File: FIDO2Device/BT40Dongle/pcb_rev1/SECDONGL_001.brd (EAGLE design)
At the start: 20.4 x 30 mm, 37 parts, among them CN1 CX60-24S-UNIT, CN2 IF_5PIN_H, CN3 IF_2PIN_SOL, SW1 SKRPACE010, SW2 SKTADAE010, U1 BT40, U2 ADP122ACPZ-3.3-R7, U3 RV-3028-C7

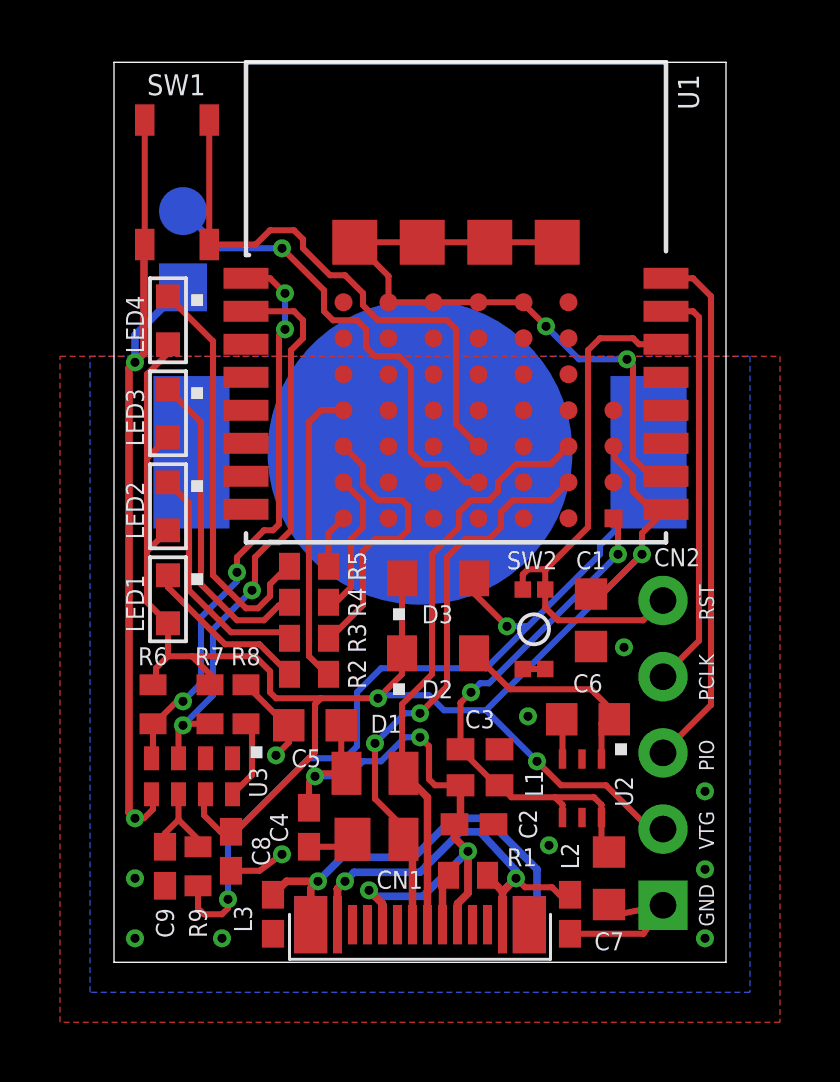
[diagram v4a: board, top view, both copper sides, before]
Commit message: 配線レイアウトを修正
・小修正
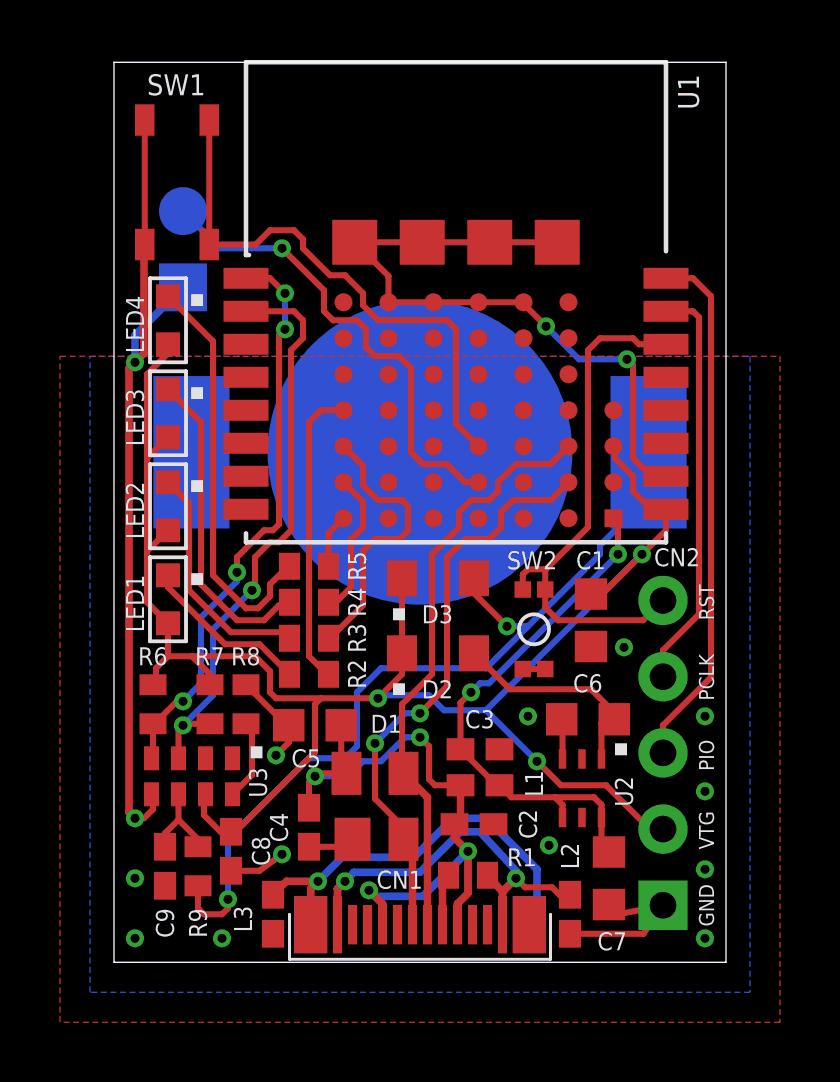
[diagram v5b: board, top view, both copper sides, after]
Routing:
- net 0V: vias 15 -> 16
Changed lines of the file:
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@@
 </element>
 <element name="C7" library="Parts" package="C0603K" value="1uF" x="16.5" y="2.8" smashed="yes" rot="R270">
-<attribute name="NAME" x="17" y="1" size="0.6" layer="25" rot="R180"/>
+<attribute name="NAME" x="17.1" y="1" size="0.6" layer="25" rot="R180"/>
 <attribute name="VALUE" x="15.00875" y="3.6" size="0.7112" layer="27" rot="R270"/>
 </element>
@@
 <wire x1="2.3" y1="22.5" x2="0.7" y2="20.9" width="0.254" layer="16"/>
 <wire x1="0.7" y1="20.9" x2="0.7" y2="20" width="0.254" layer="16"/>
+<via x="19.7" y="8.2" extent="1-16" drill="0.3"/>
 </signal>
 <signal name="VBUS_NRF">
@@
 <wire x1="16.375" y1="12.375" x2="16" y2="12.375" width="0.2032" layer="1"/>
 <wire x1="16" y1="12.375" x2="15.9" y2="12.275" width="0.2032" layer="1"/>
-<wire x1="17.6" y1="13.6" x2="17.6" y2="14.3" width="0.2032" layer="1"/>
-<wire x1="17.6" y1="14.3" x2="18.4" y2="15.1" width="0.2032" layer="1"/>
 <wire x1="16.65" y1="17.2" x2="16.7" y2="17.15" width="0.2032" layer="1"/>
 <wire x1="16.7" y1="17.15" x2="16.7" y2="16.8" width="0.2032" layer="1"/>
@@
 <wire x1="1.8" y1="10.2" x2="1.8" y2="11.3" width="0.2032" layer="1"/>
 <wire x1="1.1" y1="19.6" x2="1.1" y2="16.8" width="0.2032" layer="1"/>
-<wire x1="1.1" y1="16.5" x2="1.1" y2="13.7" width="0.2032" layer="1"/>
+<wire x1="1.1" y1="16.8" x2="1.1" y2="13.7" width="0.2032" layer="1"/>
 <wire x1="1.1" y1="13.7" x2="1.1" y2="12" width="0.2032" layer="1"/>
 <wire x1="1.1" y1="12" x2="1.8" y2="11.3" width="0.2032" layer="1"/>
 <wire x1="1.8" y1="14.4" x2="1.1" y2="13.7" width="0.2032" layer="1"/>
 <wire x1="1.8" y1="17.5" x2="1.1" y2="16.8" width="0.2032" layer="1"/>
-<wire x1="1.1" y1="16.8" x2="1.1" y2="16.5" width="0.2032" layer="1"/>
+<wire x1="17.6" y1="13.6" x2="18.4" y2="14.4" width="0.2032" layer="1"/>
+<wire x1="18.4" y1="14.4" x2="18.4" y2="15.1" width="0.2032" layer="1"/>
 </signal>
 <signal name="SW1">
@@
 <contactref element="U1" pad="16"/>
 <contactref element="CN2" pad="3"/>
-<wire x1="18.3" y1="6.98" x2="19.9" y2="8.58" width="0.2032" layer="1"/>
-<wire x1="19.9" y1="8.58" x2="19.9" y2="22.2" width="0.2032" layer="1"/>
+<wire x1="19.9" y1="9.5" x2="19.9" y2="22.2" width="0.2032" layer="1"/>
 <wire x1="18.4" y1="22.8" x2="19.3" y2="22.8" width="0.2032" layer="1"/>
 <wire x1="19.9" y1="22.2" x2="19.3" y2="22.8" width="0.2032" layer="1"/>
+<wire x1="18.3" y1="6.98" x2="18.3" y2="7.9" width="0.2032" layer="1"/>
+<wire x1="18.3" y1="7.9" x2="19.9" y2="9.5" width="0.2032" layer="1"/>
 </signal>
 <signal name="SWCLK">
 <contactref element="U1" pad="15"/>
 <contactref element="CN2" pad="4"/>
-<wire x1="18.3" y1="9.52" x2="19.5" y2="10.72" width="0.2032" layer="1"/>
-<wire x1="19.5" y1="10.72" x2="19.5" y2="21.5" width="0.2032" layer="1"/>
-<wire x1="19.5" y1="21.5" x2="19.3" y2="21.7" width="0.2032" layer="1"/>
+<wire x1="19.5" y1="11.6" x2="19.5" y2="21.5" width="0.2032" layer="1"/>
+<wire x1="18.3" y1="9.52" x2="18.3" y2="10.4" width="0.2032" layer="1"/>
+<wire x1="18.3" y1="10.4" x2="19.5" y2="11.6" width="0.2032" layer="1"/>
 <wire x1="18.4" y1="21.7" x2="19.3" y2="21.7" width="0.2032" layer="1"/>
+<wire x1="19.3" y1="21.7" x2="19.5" y2="21.5" width="0.2032" layer="1"/>
 </signal>
 <signal name="D_N">
